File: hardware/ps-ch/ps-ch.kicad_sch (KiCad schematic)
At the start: 160 parts, among them J1 Conn_02x05_Odd_Even, Q1 NMOS, Q10 Q_NPN, Q2 NMOS, Q3 Q_NPN, Q4 Q_NPN, Q5 Q_PNP, Q6 Q_PNP, Q7 Q_NPN, Q8 Q_NPN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

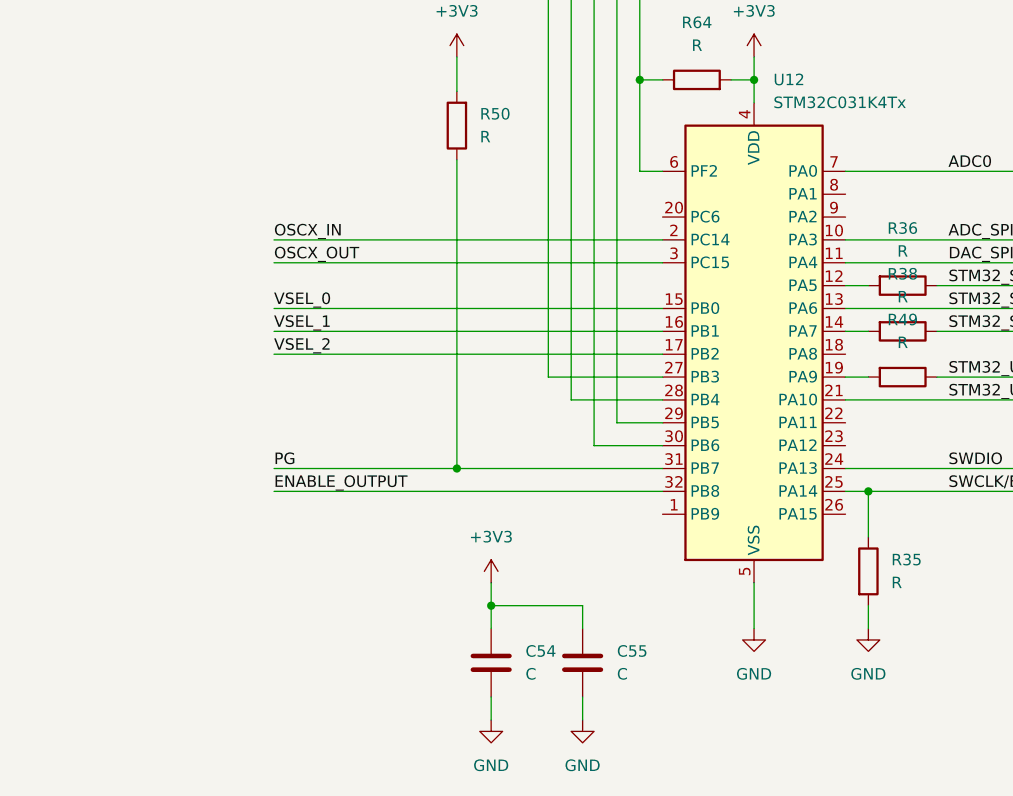
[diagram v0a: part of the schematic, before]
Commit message: Update ps-ch.kicad_sch
- added testpoints to oscx_x
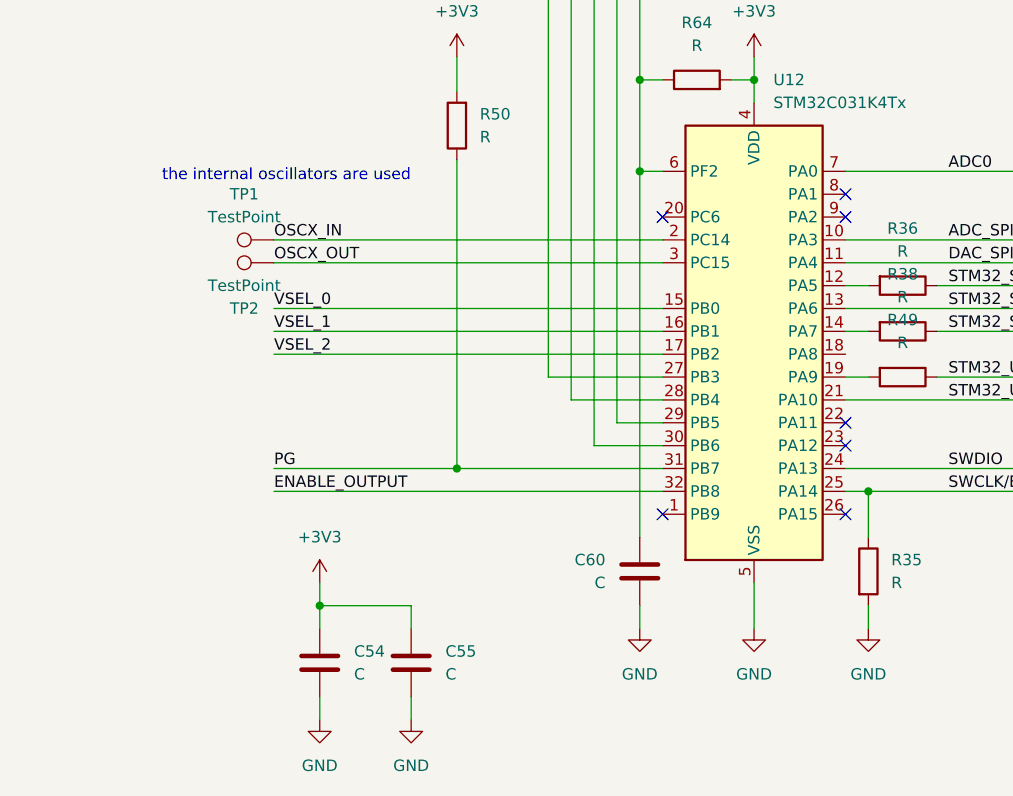
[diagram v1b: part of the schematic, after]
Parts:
- added C60: C, symbol Device:C
- added TP1, TP2: TestPoint, symbol Connector:TestPoint
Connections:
- net GND: now also C60.2
- net OSCX_IN: now also TP1.1
- net OSCX_OUT: now also TP2.1
- net STM32_NRST: now also C60.1
- no-connect marks 3 -> 10
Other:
- note added: "the internal oscillators are used"
- moved on the sheet: C54, C55

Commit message: edited schematics
- selected npn/pnp
- added connector for swd interface
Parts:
- added FL1: MSD1583-123ME_, symbol ps-ch:MSD1583-123ME_
- added R67: R, symbol Device:R
- Q10, Q3, Q4, Q7, Q8, Q9: value Q_NPN -> MMBT3904; footprint (none) -> Package_TO_SOT_SMD:SOT-23; symbol Device:Q_NPN -> Transistor_BJT:MMBT3904
- Q5, Q6: value Q_PNP -> MMBT3906; footprint (none) -> Package_TO_SOT_SMD:SOT-23; symbol Device:Q_PNP -> Transistor_BJT:MMBT3906
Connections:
- net VDDA is gone; now on net VDC: C10.1, C11.1, C41.1, C8.1, C9.1, L1.1, L4.1, L6.1, T1.7, T1.8, T1.9
- net +3V3: now also J1.3 (Pin_3), Q5.2 (E), Q6.2 (E); no longer Q5.E, Q6.E
- net Earth: now also Q3.2 (E), Q4.2 (E), Q9.2 (E), FL1.4, R67.2; no longer Q3.E, Q4.E, Q9.E
- net GND: now also J1.1 (Pin_1), J1.10 (Pin_10), J1.2 (Pin_2), J1.5 (Pin_5), J1.6 (Pin_6), J1.9 (Pin_9), Q10.2 (E), Q7.2 (E), Q8.2 (E); no longer Q10.E, Q7.E, Q8.E
- net NRST: now also J1.7 (Pin_7)
- net ON/~{OFF}: now also R67.1
- net SWCLK/BOOT0: now also J1.4 (Pin_4)
- net SWDIO: now also J1.8 (Pin_8)
- net VDC: no longer C29.1, L3.1
- net at R20.1, R60.1: now also Q9.1 (B); no longer Q9.B
- net at R45.1, R61.1: now also Q4.1 (B); no longer Q4.B
- net at R44.2, R52.2: now also Q8.1 (B); no longer Q8.B
- net at R26.2, R27.2: now also Q7.1 (B), Q8.3 (C); no longer Q7.B, Q8.C
- net at R24.1, R53.1: now also Q7.3 (C); no longer Q7.C
- net at R21.2, R22.2: now also Q5.3 (C), Q6.1 (B); no longer Q5.C, Q6.B
- net at R5.1, R54.1: now also Q6.3 (C); no longer Q6.C
- net at R65.1, R66.2: now also Q10.1 (B); no longer Q10.B
- net at R55.1, R62.1: now also Q3.1 (B); no longer Q3.B
- net at R18.2: now also Q3.3 (C); no longer Q3.C
- net at R43.2: now also Q10.3 (C); no longer Q10.C
- net at R43.1, R51.2: now also Q5.1 (B); no longer Q5.B
- net at R19.2: now also Q4.3 (C); no longer Q4.C
- net at R59.2: now also Q9.3 (C); no longer Q9.C
- new net: C29.1, FL1.3, L3.1
- new net V+: FL1.1
- new net V-: FL1.2
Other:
- note added: "SWDIO-Interface"
- note removed: "common mode choke MSD1583-123ME_"
- moved on the sheet: J1

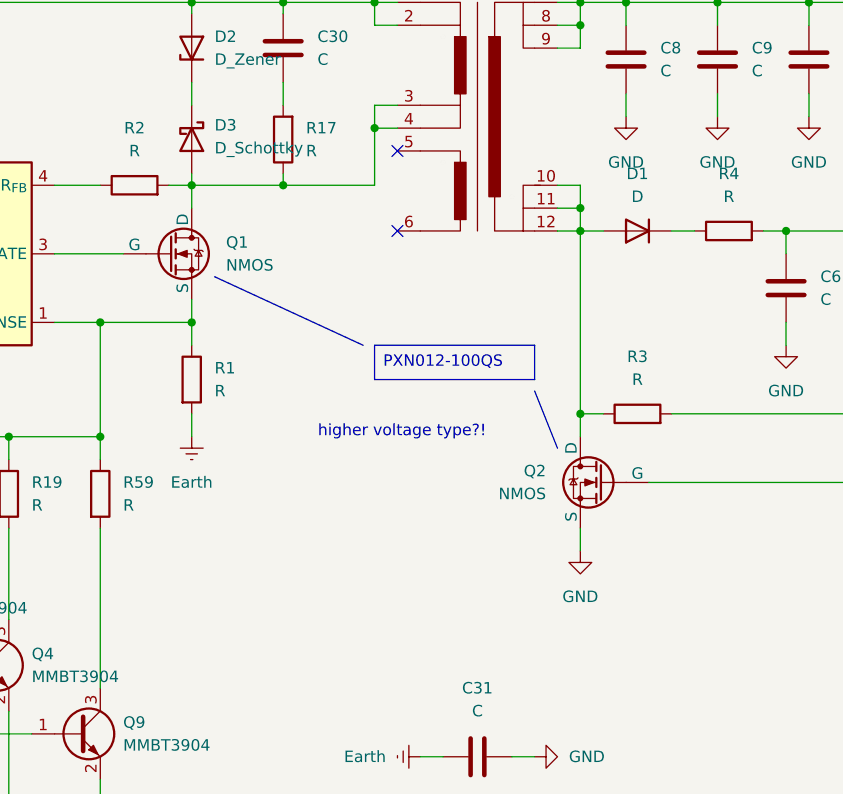
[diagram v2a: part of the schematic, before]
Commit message: added components
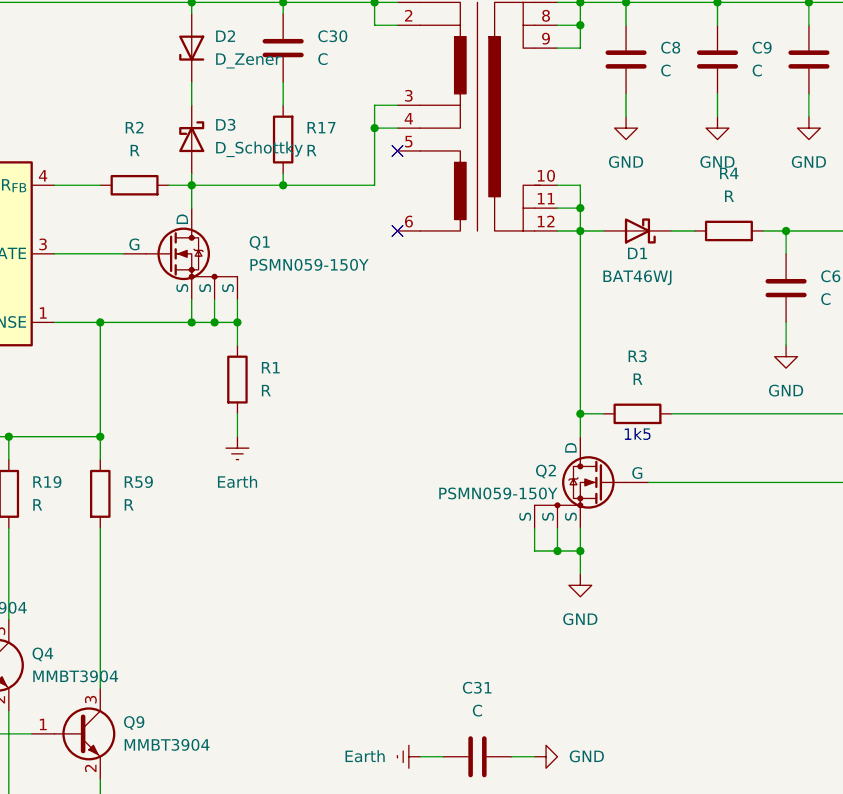
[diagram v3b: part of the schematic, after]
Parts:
- D1: value D -> BAT46WJ; symbol Device:D -> ps-ch:BAT46WJ
- Q1, Q2: value NMOS -> PSMN059-150Y; symbol Simulation_SPICE:NMOS -> ps-ch:PSMN059-150Y
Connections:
- net GND: now also Q2.1 (S), Q2.2 (S)
- net at Q1.3 (S), R1.1, R18.1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: now also Q1.1 (S), Q1.2 (S)
- net at U1.3 (GATE): now also Q1.4 (G); no longer Q1.2 (G)
- net at D3.2 (A), R17.1, R2.2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: now also Q1.5 (D); no longer Q1.1 (D)
- net at D1.2 (A), R3.1, T1.10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: now also Q2.5 (D); no longer Q2.1 (D)
- net at U2.1 (GATE): now also Q2.4 (G); no longer Q2.2 (G)
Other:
- note added: "1k5"
- note removed: "higher voltage type?!"
- moved on the sheet: R1

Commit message: started making hierachical design
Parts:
- removed C1, C10, C11, C2, C26, C27, C28, C29, C3, C30, C31, C4, C5, C54, C55, C58, C59, C6, C60, C7, C8, C9: C, symbol Device:C
- removed D1: BAT46WJ, symbol ps-ch:BAT46WJ
- removed D2: D_Zener, symbol Device:D_Zener
- removed D3: D_Schottky, symbol Device:D_Schottky
- removed FL1: MSD1583-123ME_, symbol ps-ch:MSD1583-123ME_
- removed J1: Conn_02x05_Odd_Even, symbol Connector_Generic:Conn_02x05_Odd_Even
- removed L3: L, symbol Device:L
- removed Q1, Q2: PSMN059-150Y, symbol ps-ch:PSMN059-150Y
- removed Q3, Q4, Q9: MMBT3904, Package_TO_SOT_SMD:SOT-23, symbol Transistor_BJT:MMBT3904
- removed R1, R17, R18, R19, R2, R3, R35, R36, R38, R39, R4, R41, R45, R49, R55, R59, R60, R62, R64: R, symbol Device:R
- removed T1: 750311590, symbol ps-ch:750311590
- removed TP1, TP2: TestPoint, symbol Connector:TestPoint
- removed U1: LT8306, Package_TO_SOT_SMD:TSOT-23-6, symbol ps-ch:LT8306
- removed U12: STM32C031K4Tx, Package_QFP:LQFP-32_7x7mm_P0.8mm, symbol MCU_ST_STM32C0:STM32C031K4Tx
- removed U14: ADS1118IDGS, symbol Analog_ADC:ADS1118IDGS
- removed U2: LT8309, symbol ps-ch:LT8309
- removed U4: AD5693RBCPZ, symbol ps-ch:AD5686RBCPZ
- added C61, C68: C, symbol Device:C
- added L9: L, symbol Device:L
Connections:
- net ENABLE_PWR_SPL is gone; now on net STM32/ENABLE_PWR_SPL: U3.13 (EN)
- net FPWM/~{PFM} is gone; now on an unnamed net: R42.2
- net Earth: no longer R61.2
- net GND: now also R61.2, C61.2, C68.2; no longer R28.2
- net VDC: now also C61.1
- net Flyback Converter/V_PREREG_EQUIV_PWM: now reaches R20.1
- net at R10.1, R11.2, U3.12 (SYNC/MODE): no longer R42.1
- net DAC/VOUTA: now reaches U5.1 (+)
- net DAC/VOUTB: now reaches U8.1 (+)
- net DAC/VOUTB: no longer R28.1
- net DAC/VOUTC: now reaches U6.3 (LIMIT), U7.1 (+)
- net STM32/ENABLE_PWR_SPL: now reaches R61.1
- net at C15.1, C16.1, C17.1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: now also L9.1
- net Switch/ON: now reaches U10.6 (VOD)
- net Switch/ON: now also R28.2
- net Switch/OUT: now reaches R23.1, U6.8 (IN+)
- net Switch/OFF: now reaches U6.6 (~{ALERT})
- net DISABLE_VOLTAGE_SENSING renamed STM32/DISABLE_VOLTAGE_SENSING
- net FUSE/~{CURRENT_LIMITING}_MODE renamed STM32/FUSE/~{CURRENT_LIMITING}_MODE
- net STM32_NRST renamed STM32/~{STM32_RST}
- net STM32_UART_RX renamed STM32/STM32_UART_RX
- net STM32_UART_TX renamed STM32/STM32_UART_TX
- net SWCLK/BOOT0 renamed STM32/ACTIVATE_BOOTLOADER
- net VSEL_0 renamed STM32/STM32_TIM1_CH1_PWM
- net VSEL_1: no longer names the net of U10.4 (VIB)
- net VSEL_2: no longer names the net of U10.5 (VIC)
- new net STM32/ENABLE_OUTPUT: R28.1
- new net STM32/FPWM/~{PFM}: R42.1
- new net Switch/IN: C68.1, L9.2
- no-connect marks 10 -> 0
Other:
- added sheet ADC (adc.kicad_sch)
- added sheet DAC (dac.kicad_sch)
- added sheet Flyback Converter (flyback_converter.kicad_sch)
- added sheet STM32 (stm32.kicad_sch)
- added sheet Switch (switch.kicad_sch)
- note removed: "- STM32 is programmed via USART1 (PA9/PA10) - the bootloader is activated by applying pattern 11 -> BOOT_LOCK(bit) = 0, nBOOT1(bit) = 1, BOOT0(pin) = 1, nBOOT0_SEL(bit) = 0"
- note removed: "0..2.5V"
- note removed: "1k5"
- note removed: "SWDIO-Interface"
- note removed: "can drive 2k || 10nF"
- note removed: "the internal oscillators are used"
- note removed: "wire with ENABLE_OUTPUT"
- moved on the sheet: C12, C13, C14, C15, C16, C17, C18, C19, C20, C21, C22, C23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

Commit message: created voltage regulation
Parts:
- removed C32, C35, C37, C38, C40, C44, C45: C, symbol Device:C
- removed Q10, Q7, Q8: MMBT3904, Package_TO_SOT_SMD:SOT-23, symbol Transistor_BJT:MMBT3904
- removed Q5, Q6: MMBT3906, Package_TO_SOT_SMD:SOT-23, symbol Transistor_BJT:MMBT3906
- removed R21, R22, R24, R25, R26, R27, R37, R40, R43, R44, R5, R51, R52, R53, R54, R65, R66: R, symbol Device:R
- removed U7, U8: OPA992IDCKR, symbol ps-ch:OPA992IDCKR
- added R62: R, symbol Device:R
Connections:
- net Switch/ON: no longer U10.6 (VOD)
- net Voltage Regulation/VFB: now reaches C25.2, R12.1, R13.2, R14.2, R15.1, R16.2, U3.7 (FB)
- net Voltage Regulation/VFB: now also R62.2
- net Voltage Regulation/VSENSE_SCALED: now reaches C39.1, R29.1, U9.4
- net at R14.1, U5.3 (-), U5.4: now also R62.1
- net Voltage Regulation/CURRENT: now reaches U6.2 (OUT)
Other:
- added sheet Voltage Regulation (voltage_regulation.kicad_sch)
- note added: "?!?!"
- note added: "scale down to max. 2.5V"
- note removed: "CURRENT LIMITER"
- note removed: "VOLTAGE ADJUSTMENT (VSENSE)"
- note removed: "scale down to 0..2.5V"

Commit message: did some wiring
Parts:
- removed C36, C39, C42, C43, C68: C, symbol Device:C
- removed R23, R29, R30, R31, R32, R33, R34: R, symbol Device:R
- removed U6: INA301A3, symbol ps-ch:INA301A3
- removed U9: OPA992IDCKR, symbol ps-ch:OPA992IDCKR
- added C68: C_Polarized, symbol Device:C_Polarized
- added C76: C, symbol Device:C
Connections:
- net Switch/IN is gone; now on net ADC/AIN0: L9.2
- net ADC/AIN0: now also C68.1
- net GND: now also C68.2, C76.2
- net STM32/ENABLE_OUTPUT: no longer R28.1
- net Switch/ARM_OUTPUT: now reaches U10.6 (VOD)
- net ON/~{OFF} renamed ARM_OUTPUT
- net Switch/ON renamed Current Measurement/~{ALERT}
- new net Current Measurement/OUT: C76.1
- new net Current Measurement/RESET: R28.1
- no-connect marks 0 -> 1
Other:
- sheet Voltage Regulation renamed Voltage Correction
- added sheet Current Measurement (current_measurement.kicad_sch)
- sheet Switch ports: added ARM_OUTPUT, ON/~{OFF}, ~{OVC}; removed OFF, ON
- sheet Voltage Correction: file voltage_regulation.kicad_sch -> voltage_correction.kicad_sch
- sheet Voltage Correction ports: added VREF+, VSENSE, VSENSE+, VSENSE-; removed VSENSE_SCALED
- note added: "if 'FUSE' Mode is set, it simultaneously pulls up the ~{ALERT} Pin otherwise it is pulled low"
- note added: "scaling, tbd!!!"
- note removed: "?!?!"
- note removed: "FUSE .. Mode and \ALERT must be and-connected"
- note removed: "connect left or right to the relay?"
- note removed: "input filter!"
- note removed: "maybe use diff-amp with laser trimmed r"
- note removed: "scale down to max. 2.5V"

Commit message: drawn enabled circuit
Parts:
- removed R28: R, symbol Device:R
- added Q11: MMBT3904, Package_TO_SOT_SMD:SOT-23, symbol Transistor_BJT:MMBT3904
- added R75: R, symbol Device:R
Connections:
- net ADC/AIN0: now also R75.2
- net GND: now also Q11.2 (E)
- new net: Q11.3 (C), R75.1
- new net STM32/DISCHARGE_OUTPUT: Q11.1 (B)
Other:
- sheet STM32 ports: added DISCHARGE_OUTPUT, ~{OCP}; removed none
- sheet Switch ports: added MODE, ~{OCP}; removed ~{OVC}
- note added: "add discharge circuit"
- note removed: "if 'FUSE' Mode is set, it simultaneously pulls up the ~{ALERT} Pin otherwise it is pulled low"
- moved on the sheet: C76

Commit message: added 74LVC126A
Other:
- note removed: "add discharge circuit"
- moved on the sheet: C76, Q11, R75
